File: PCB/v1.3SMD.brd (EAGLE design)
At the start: 80 x 80 mm, 34 parts, among them IC2 ATMEGA328PUA

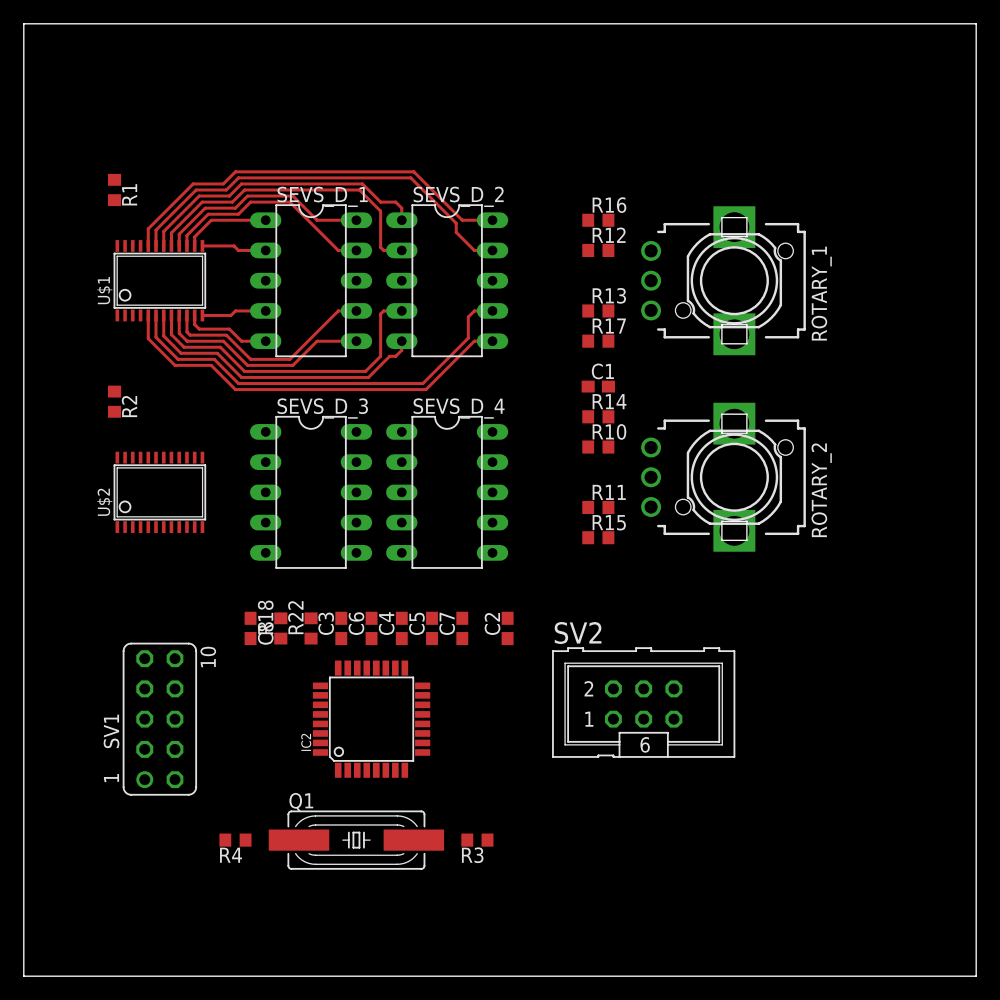
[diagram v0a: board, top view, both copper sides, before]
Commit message: added resistors
added resistors to data lines for current limitation. You could also add
capacitors in order to have a low pass filter but I rely on the gat
input capacity of the ICs instead.
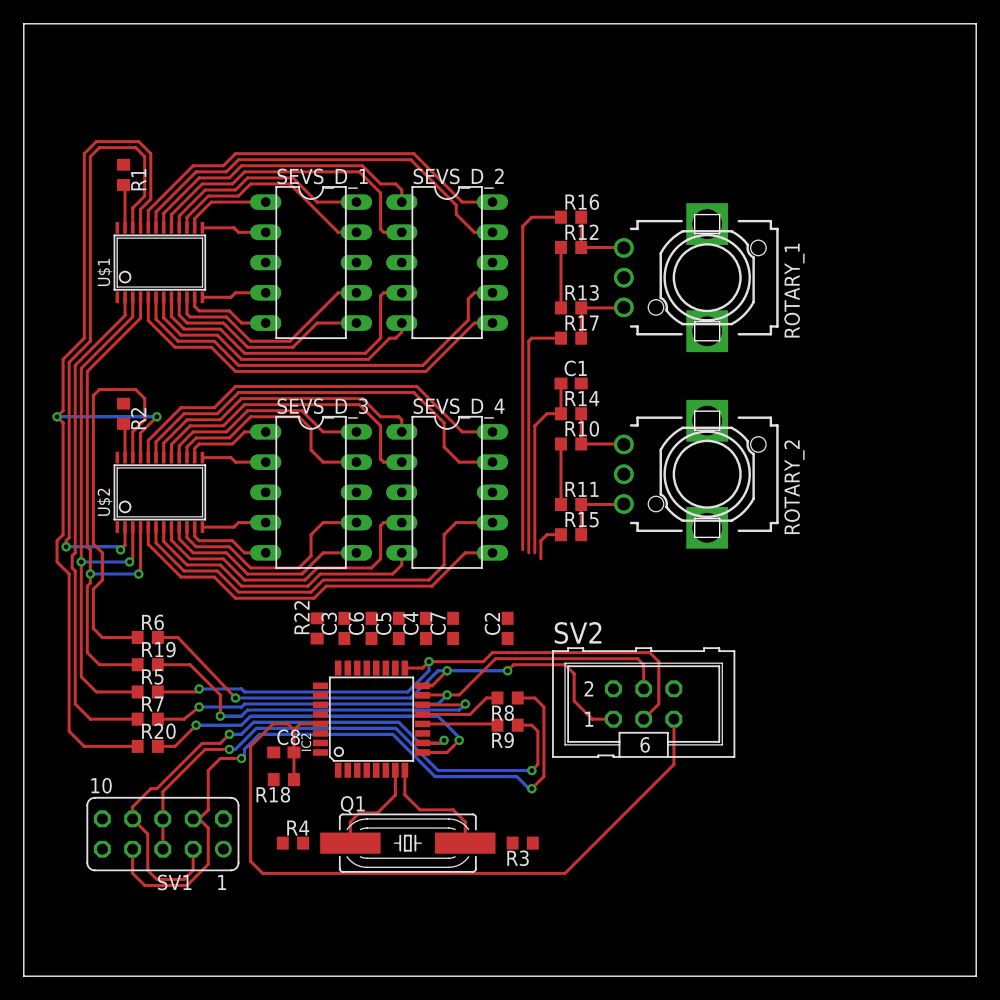
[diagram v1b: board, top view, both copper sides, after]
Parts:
- added R19, R20, R5, R6, R7, R8, R9: 82k, rcl:R0603
- moved R18 12.7 mm to (21.8, 16.5), turned to 180 degrees
- moved C8 10.8 mm to (21.8, 18.8), turned to 0 degrees
- moved SV1 9.66 mm to (11.7, 11.9), turned to 180 degrees
- moved R4 4.83 mm to (22.6, 11.2), turned to 0 degrees
- moved Q1 4.33 mm to (32.3, 11.2)
- moved R3 3.82 mm to (41.9, 11.2)
- moved C5 2.79 mm to (31.5, 29.2)
- moved R11 2.30 mm to (46.0, 39.6)
- moved R15 2.30 mm to (46.0, 37.1)
- moved C1 2.30 mm to (46.0, 49.8)
- moved R10 2.30 mm to (46.0, 44.7)
- moved R12 2.30 mm to (46.0, 61.2)
- moved R13 2.30 mm to (46.0, 56.1)
- moved R14 2.30 mm to (46.0, 47.2)
- moved R16 2.30 mm to (46.0, 63.8)
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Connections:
- removed net I1: SV2.3
- removed net I2: SV2.1
- removed net I3: SV2.4
- new net LE: R19.1, U$1.4, U$2.4
- new net LE_M: IC2.14, R19.2
- new net MISO: R6.1, U$2.22
- new net MISO_M: IC2.16, R6.2, SV2.1
- new net MOSI: R7.1, U$1.2
- new net MOSI_M: IC2.15, R7.2, SV2.4
- new net N$10: IC2.28
- new net N$12: IC2.27
- new net N$13: IC2.11
- new net N$17: IC2.31
- new net N$18: IC2.30
- new net N$19: IC2.19
- new net N$20: IC2.22
- new net N$22: U$1.22, U$2.2
- new net PWCLK: R20.1, U$1.21, U$2.21
- new net PWCLK_M: IC2.9, R20.2
- new net SCK: R5.1, U$1.3, U$2.3
- new net SCK_M: IC2.17, R5.2, SV2.3
- new net SCL_M: IC2.12, R9.2
- new net SDA_M: IC2.13, R8.2
- net RE1_1: now also IC2.23; no longer IC2.17
- net RE1_2: now also IC2.24; no longer IC2.16
- net RE2_1: now also IC2.32; no longer IC2.24
- net RE2_2: now also IC2.1; no longer IC2.23
- net SCL: now also R9.1; no longer IC2.12
- net SDA: now also R8.1; no longer IC2.13
- net SEVS3_1: now also U$2.14; no longer U$2.5
- net SEVS3_2: now also U$2.13; no longer U$2.6
- net SEVS3_3: now also U$2.12; no longer U$2.7
- net SEVS3_4: now also U$2.11; no longer U$2.8
- net SEVS3_5: now also U$2.16; no longer U$2.9
- net SEVS3_6: now also U$2.15; no longer U$2.10
- net SEVS3_7: now also U$2.10; no longer U$2.11
- net SEVS3_8: now also U$2.9; no longer U$2.12
- net SEVS4_1: now also U$2.18; no longer U$2.13
- net SEVS4_2: now also U$2.17; no longer U$2.14
- net SEVS4_3: now also U$2.8; no longer U$2.15
- net SEVS4_4: now also U$2.7; no longer U$2.16
- net SEVS4_5: now also U$2.20; no longer U$2.17
- net SEVS4_6: now also U$2.19; no longer U$2.18
- net SEVS4_7: now also U$2.6; no longer U$2.19
- net SEVS4_8: now also U$2.5; no longer U$2.20
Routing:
- net PWCLK: track 0.00 -> 82.0 mm, vias 0 -> 2
- net RESET: track 0.00 -> 64.5 mm
- net SDA: track 0.00 -> 59.0 mm, vias 0 -> 2
- net SCK_M: track 0.00 -> 52.0 mm, vias 0 -> 2
- net N$22: track 0.00 -> 51.9 mm, vias 0 -> 2
- net MISO_M: track 0.00 -> 47.4 mm, vias 0 -> 3
- net MOSI_M: track 0.00 -> 47.2 mm, vias 0 -> 2
- net SCK: track 0.00 -> 46.0 mm, vias 0 -> 2
- net SCL: track 0.00 -> 44.9 mm, vias 0 -> 2
- net LE: track 0.00 -> 44.6 mm, vias 0 -> 2
- net CH_LVL: track 0.00 -> 43.9 mm, vias 0 -> 2
- net MOSI: track 0.00 -> 41.9 mm
- net SEVS4_7: track 0.00 -> 35.2 mm
- net SEVS4_6: track 0.00 -> 34.9 mm
- net MISO: track 0.00 -> 34.4 mm
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
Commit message: Finished routing
connected all air wires and finished placing. Still need to finish up
labels and positions in silk screen
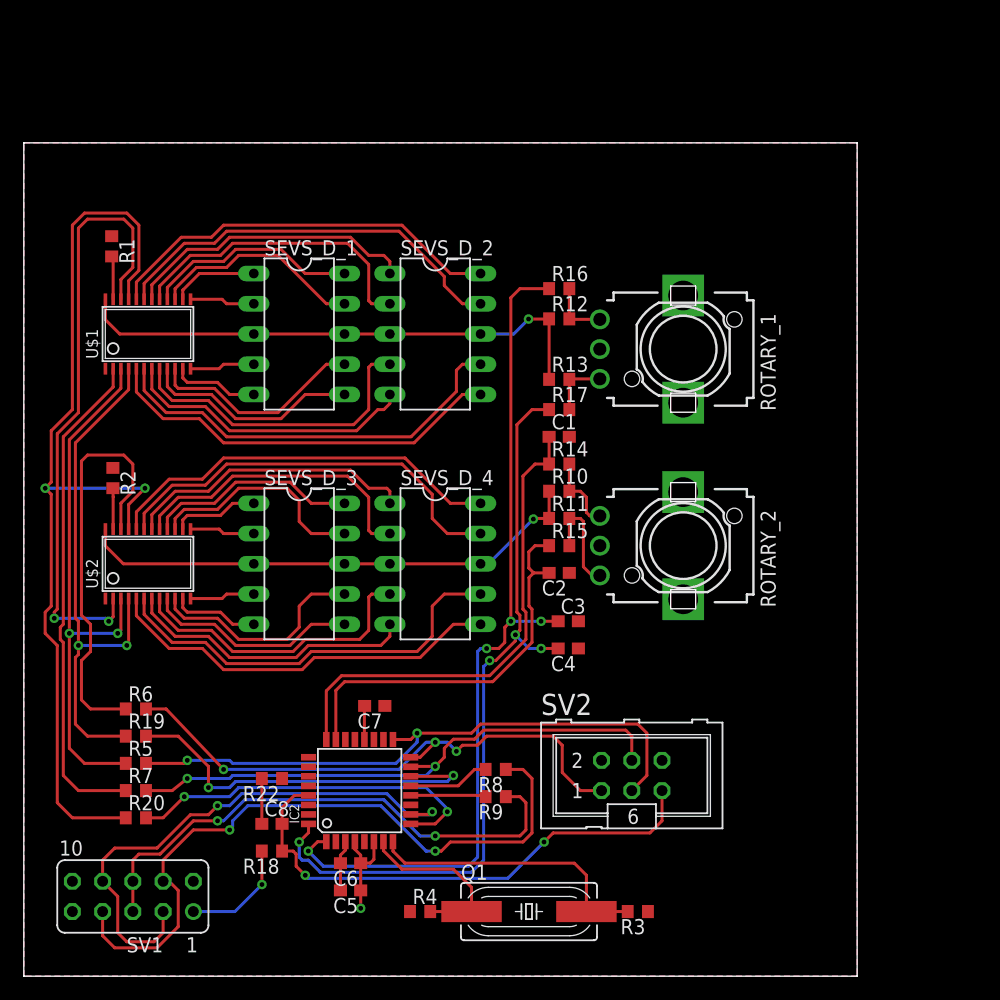
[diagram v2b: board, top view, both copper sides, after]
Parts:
- moved C5 22.4 mm to (27.4, 7.21), turned to 180 degrees
- moved C6 19.8 mm to (27.4, 9.49), turned to 180 degrees
- moved C3 18.8 mm to (45.7, 29.8), turned to 0 degrees
- moved R22 13.2 mm to (20.8, 16.6), turned to 180 degrees
- moved R4 12.1 mm to (33.3, 5.43)
- moved C4 12.1 mm to (45.7, 27.5), turned to 180 degrees
- moved Q1 11.7 mm to (42.4, 5.43)
- moved R3 11.2 mm to (51.6, 5.43)
- moved C7 9.26 mm to (29.5, 22.7), turned to 180 degrees
- moved C2 6.37 mm to (45.0, 33.9), turned to 180 degrees
- moved ROTARY_1 6.33 mm to (55.4, 52.7)
- moved ROTARY_2 6.33 mm to (55.4, 36.2)
- moved R18 6.08 mm to (20.8, 10.5)
- moved C8 6.08 mm to (20.8, 12.8)
- moved IC2 6.08 mm to (28.2, 15.6)
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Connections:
- net RE1_1: now also IC2.24; no longer IC2.23
- net RE1_2: now also IC2.23; no longer IC2.24
- net RE2_1: now also IC2.1; no longer IC2.32
- net RE2_2: now also IC2.32; no longer IC2.1
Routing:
- net VCC: track 10.2 -> 106.4 mm, vias 0 -> 4
- net RE2_2: track 20.6 -> 65.1 mm, vias 0 -> 4
- net RE2_1: track 30.7 -> 73.5 mm, vias 0 -> 4
- net RE1_2: track 3.42 -> 33.5 mm
- net RE1_1: track 15.8 -> 41.4 mm
- net RESET: track 64.5 -> 44.3 mm, vias 0 -> 2
- net N$8: track 9.86 -> 24.4 mm
- net N$7: track 8.58 -> 14.9 mm
- net GND: track 0.00 -> 4.26 mm
- net N$2: track 0.00 -> 3.81 mm
- net N$1: track 6.14 -> 9.06 mm
- net N$15: track 0.00 -> 2.83 mm
- net CH_LVL: track 43.9 -> 45.6 mm
- net N$6: track 6.14 -> 5.12 mm
- net N$5: track 6.14 -> 5.12 mm
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- added copper zone on layer 1, net GND
- added copper zone on layer 16, net VCC
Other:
- board size 80 x 80 mm -> 70 x 70 mm
